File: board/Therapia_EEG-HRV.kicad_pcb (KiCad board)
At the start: 4 copper layers, 61.8 x 45 mm, 141 parts, among them J1 USB-C_16P, J2 Header_2x6

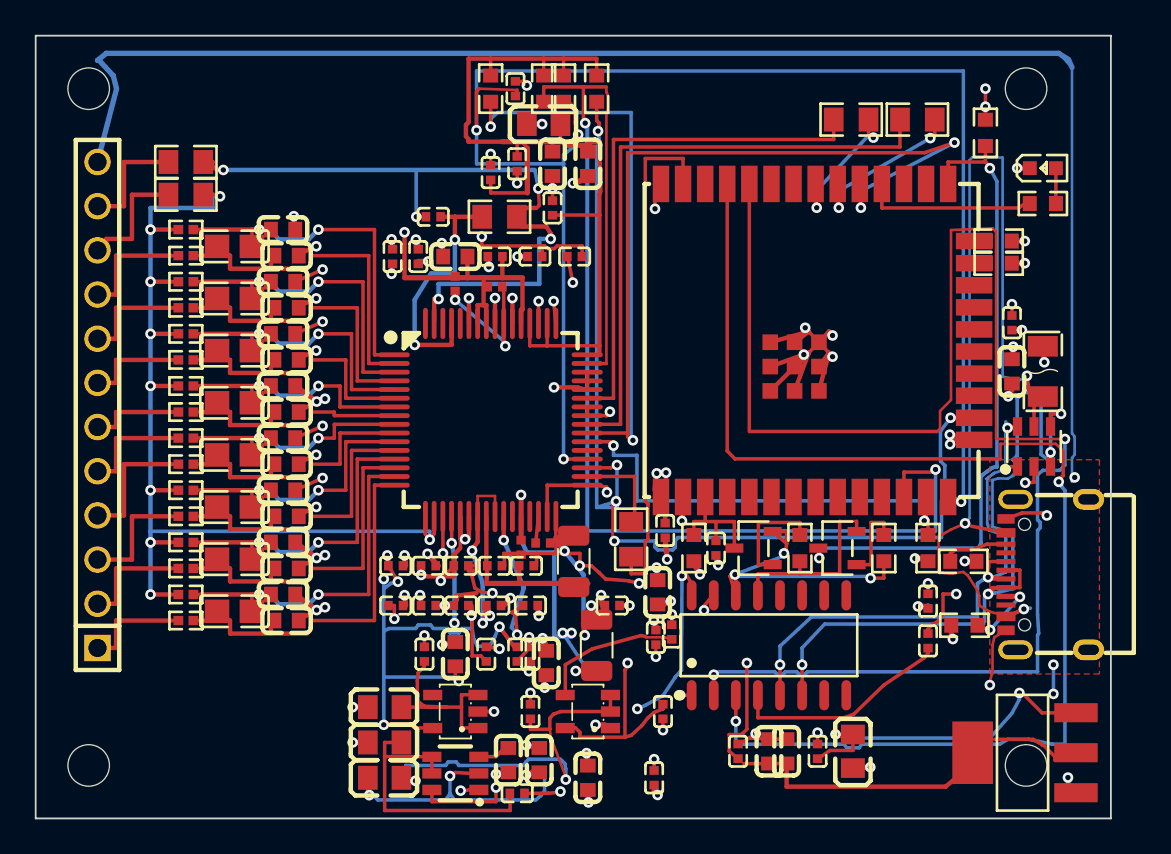
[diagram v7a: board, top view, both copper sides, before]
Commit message: Y9 re-export after the QA MINORs: S7p before S7v, S7m and S7_maskweb wired, all gates green
run.sh: S7p now runs before S7v (clipped paste no longer inflates the
openings S7v keeps clear of), S7m after S7d, S7_maskweb after S7_paste.
Via counts 237 -> 232 (IPC-D-356 / ODB++ constants). ACCEPTANCE addendum 5
(I at 0.10 mm, L), STATUS. Board and fab regenerated from the pre-S7v
board: DRC 0/0, dangling 0, via-to-opening min 0.1007 mm, no different-net
dam under 0.10 mm, IN1P-IN8N path change <= 0.0013 mm.

Co-Authored-By: Claude Opus 5.5 (1M context) <noreply@anthropic.com>
Claude-Session: https://claude.ai/code/session_01BbaSxDrhhKaR1T3EhiM8tM
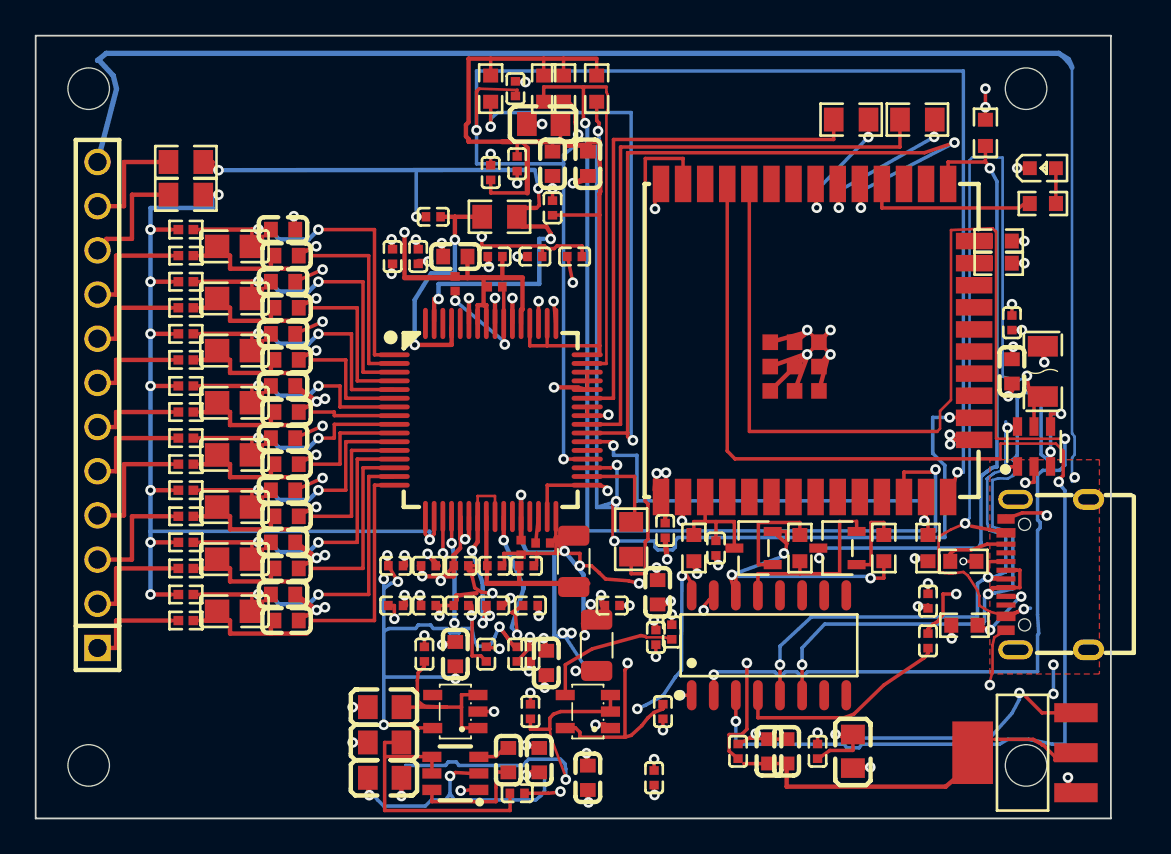
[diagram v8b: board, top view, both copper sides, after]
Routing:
- net ADS_RESET_N: track 92.4 -> 90.7 mm
- net ADS_PWDN_N: track 60.5 -> 61.6 mm
- net SPI_MISO: track 9.01 -> 8.43 mm
- net GND: track 131.3 -> 131.9 mm
- net LM_CAP_P: vias 2 -> 0
